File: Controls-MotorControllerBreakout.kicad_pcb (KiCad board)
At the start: 2 copper layers, 54.5 x 51.5 mm, 59 parts, among them J1 MC CAN 1, J2 MC CAN 2, J3 CTRLS, J4 EXT PWR, J5 CANDAPTER, J6 FAN 1, J7 FAN 2, Q1 PMV35EPER, Q2 PMV35EPER, Q3 RUM001L02T2CL, Q4 RE1C001ZPTL, U1 TPS2121RUXR

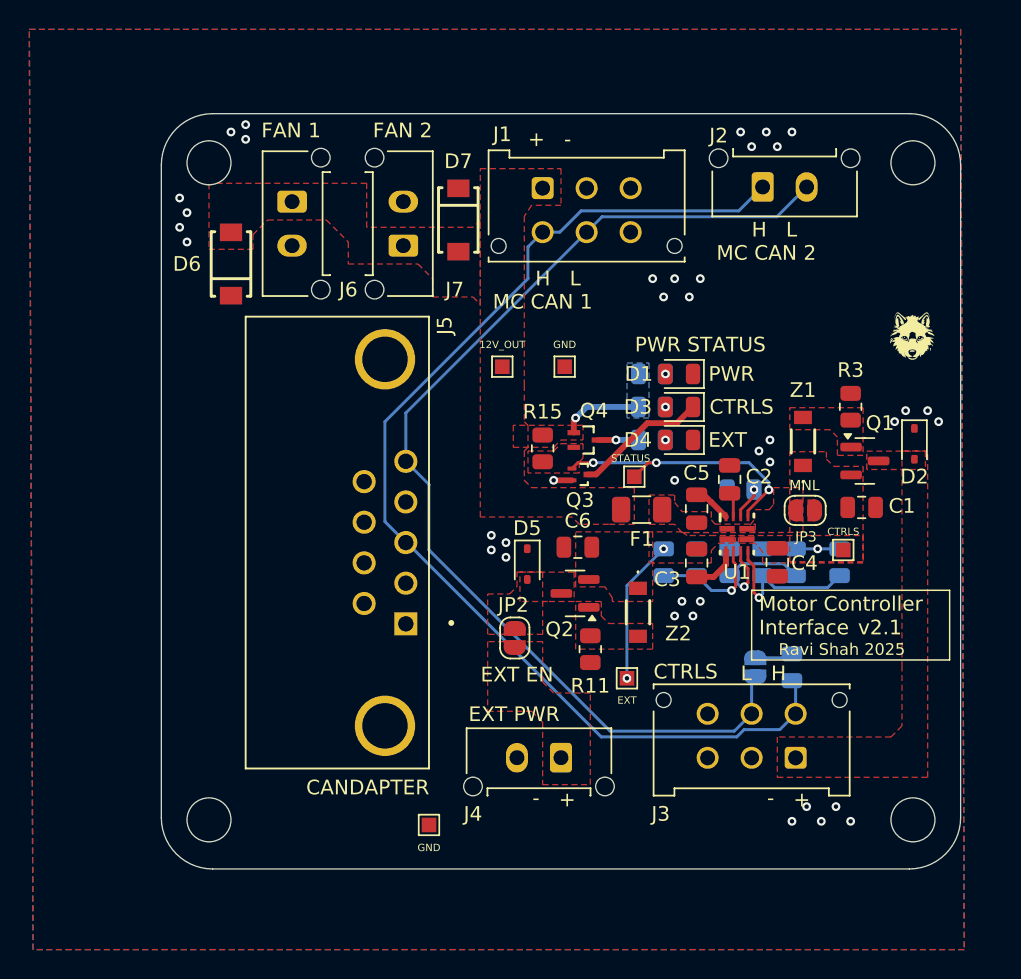
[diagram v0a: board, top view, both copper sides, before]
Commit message: modify for PEAK candapter
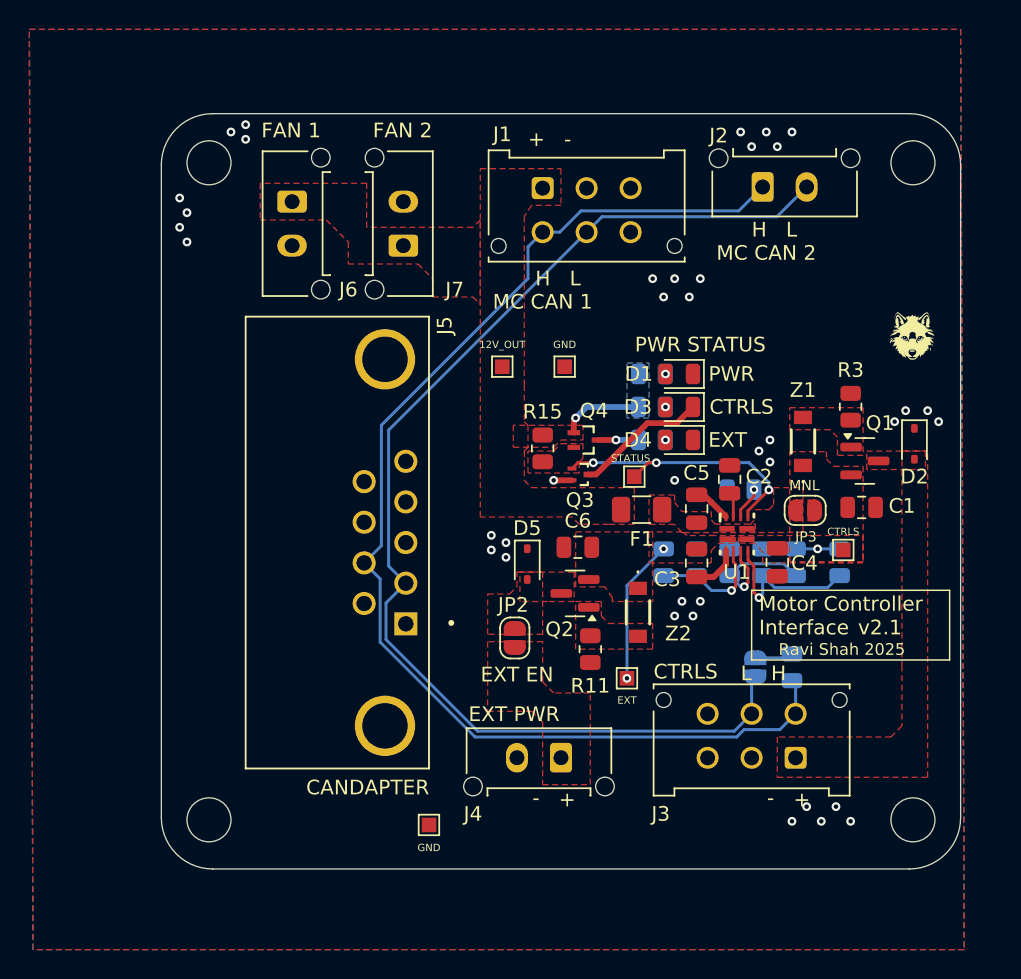
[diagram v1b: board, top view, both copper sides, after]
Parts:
- removed D6: FLYBK1, UTSVT_Passive:DO-221AC
- removed D7: FLYBK2, UTSVT_Passive:DO-221AC
- G***: moved to F.Cu
- moved G*** 4.65 mm to (68.8, 68.8), turned to -90 degrees
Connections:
- J5 pad 2: unconnected-(J5-Pad2) -> /CAN_L
- J5 pad 3: /CAN_H -> unconnected-(J5-Pad3)
- J5 pad 5: /CAN_L -> unconnected-(J5-Pad5)
- J5 pad 7: unconnected-(J5-Pad7) -> /CAN_H
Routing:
- net /CAN_L: track 73.9 -> 81.5 mm
- net /CAN_H: track 77.6 -> 83.7 mm
